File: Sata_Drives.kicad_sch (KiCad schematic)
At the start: 66 parts

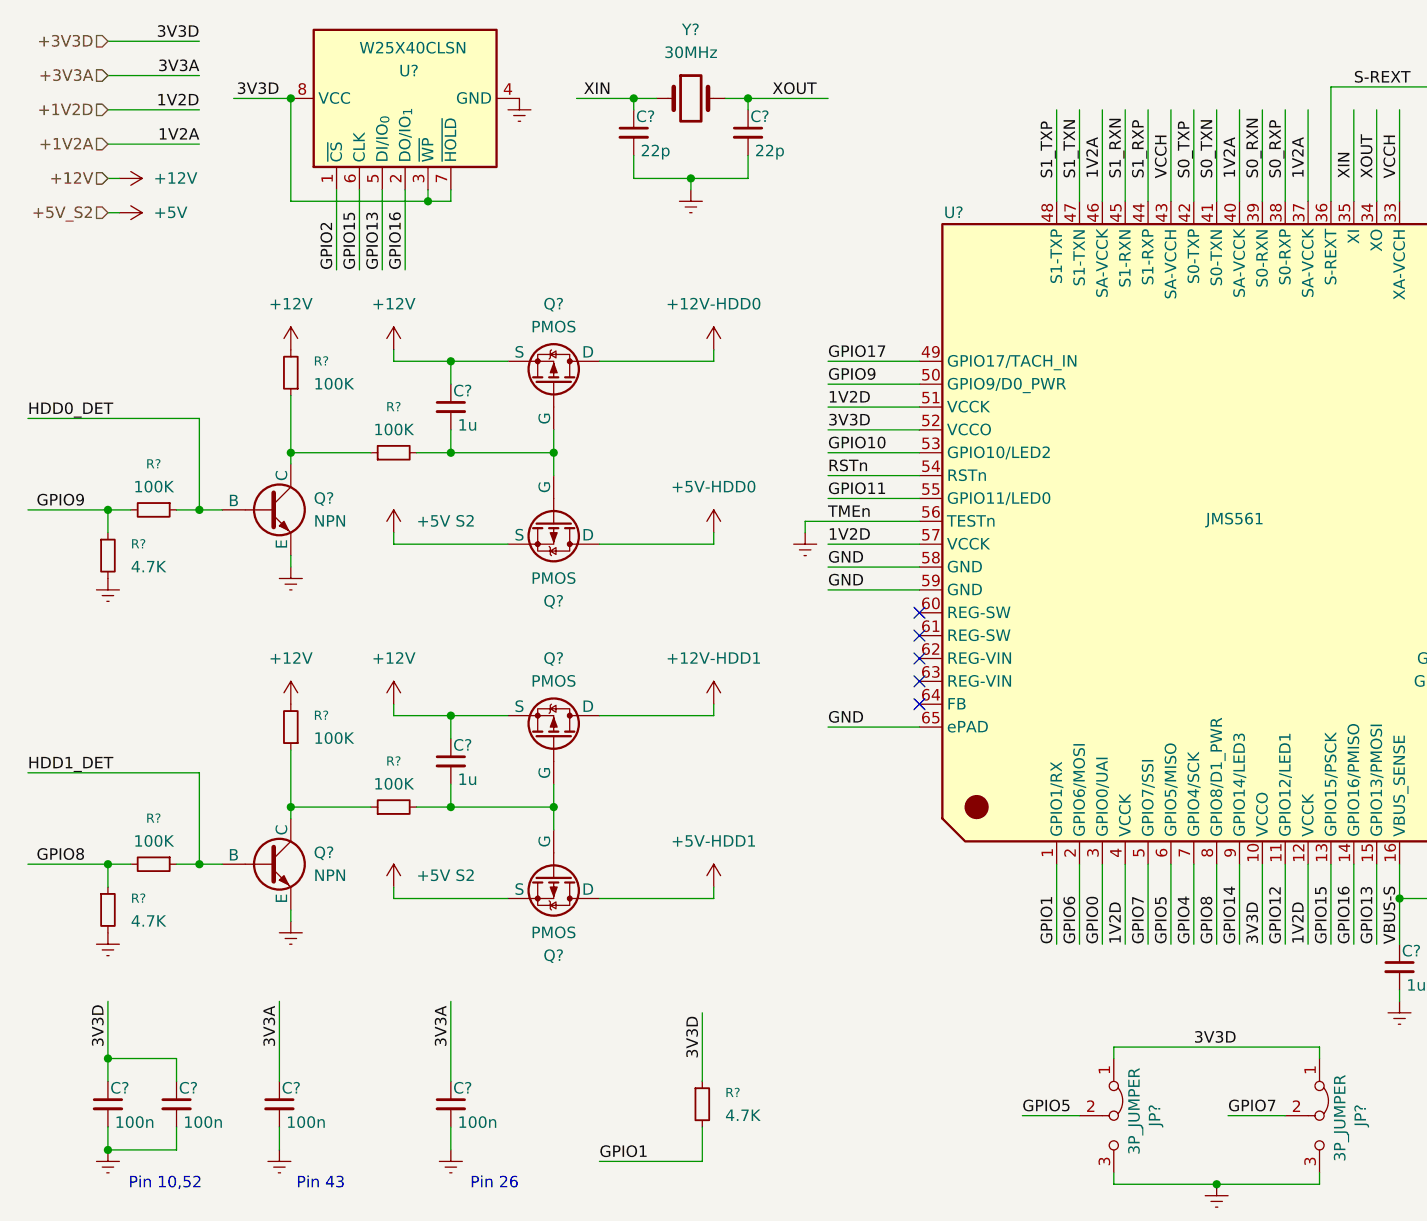
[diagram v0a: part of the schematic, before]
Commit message: Removed Ethernet
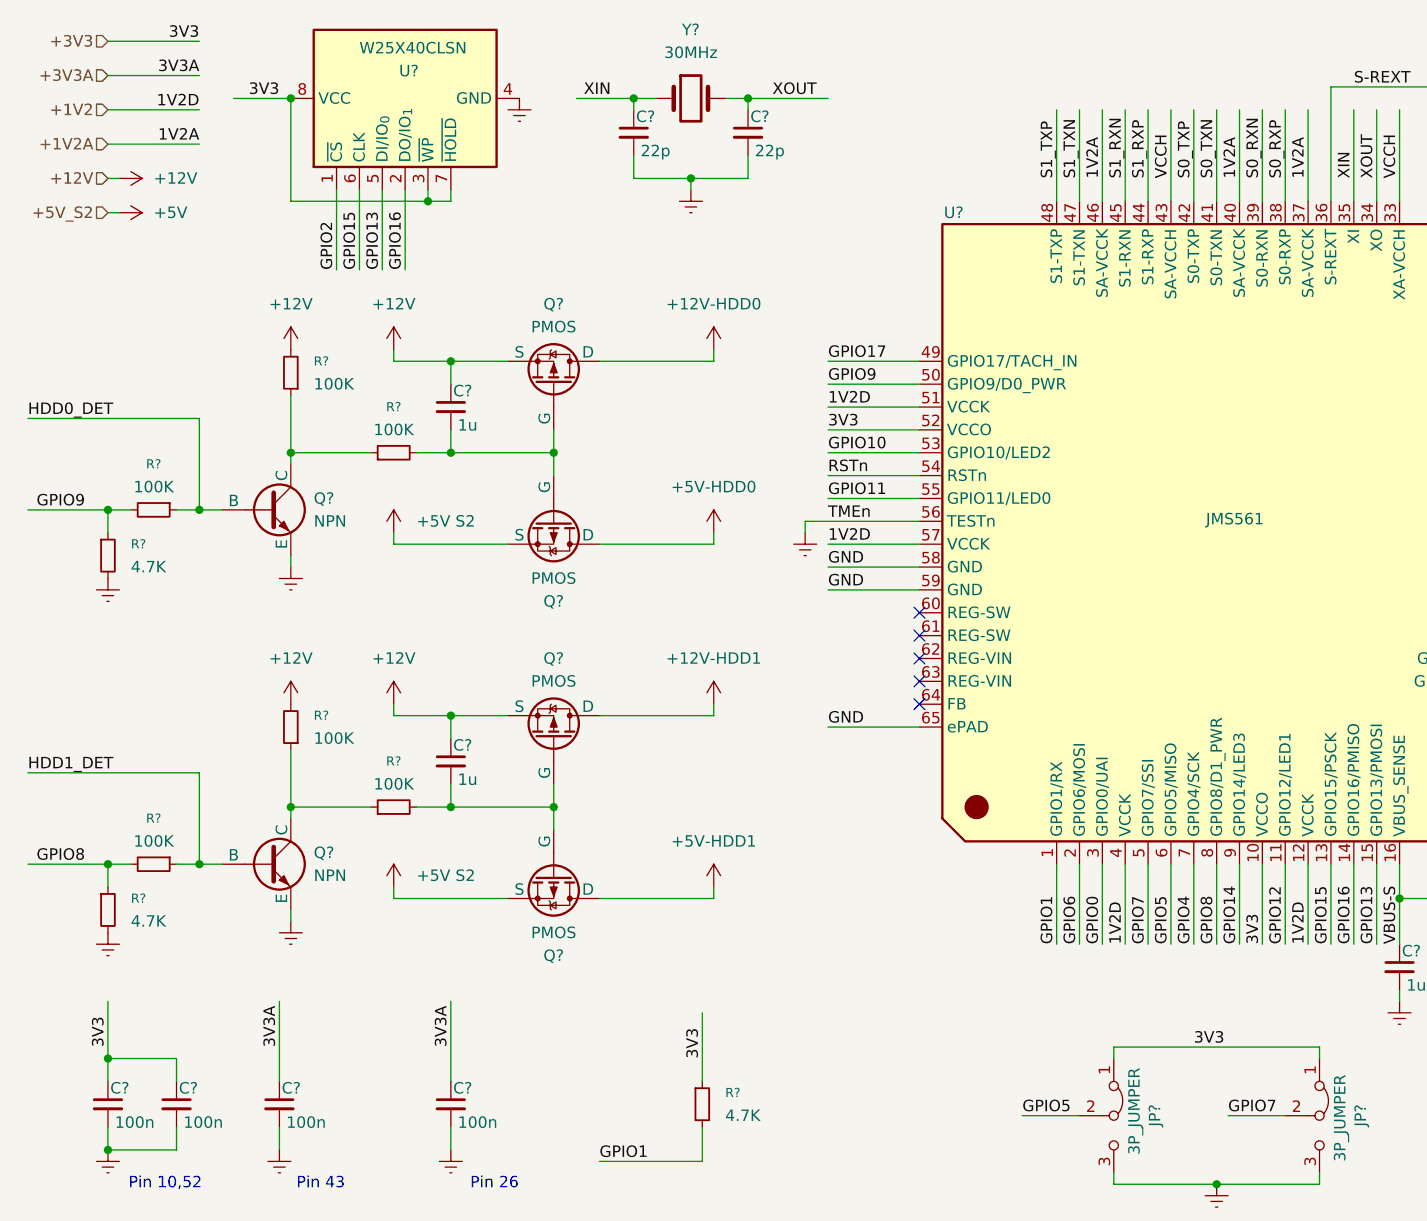
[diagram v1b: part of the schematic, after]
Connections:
- net +1V2D renamed +1V2
- net +3V3D renamed +3V3
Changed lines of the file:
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@@
 		)
 	)
-	(label "3V3D"
+	(label "3V3"
 		(at 34.29 15.24 180)
 		(effects
@@
 		)
 	)
-	(label "3V3D"
+	(label "3V3"
 		(at 144.78 127 0)
 		(effects
@@
 		)
 	)
-	(label "3V3D"
+	(label "3V3"
 		(at 24.13 127 90)
 		(effects
@@
 		)
 	)
-	(label "3V3D"
+	(label "3V3"
 		(at 90.17 128.27 90)
 		(effects
@@
 		)
 	)
-	(label "3V3D"
+	(label "3V3"
 		(at 43.18 21.59 180)
 		(effects
@@
 		)
 	)
-	(label "3V3D"
+	(label "3V3"
 		(at 152.4 115.57 90)
 		(effects
@@
 		)
 	)
-	(label "3V3D"
+	(label "3V3"
 		(at 104.14 58.42 0)
 		(effects
@@
 		)
 	)
-	(hierarchical_label "+1V2D"
+	(hierarchical_label "+1V2"
 		(shape input)
 		(at 24.13 22.86 180)
@@
 		)
 	)
-	(hierarchical_label "+3V3D"
+	(hierarchical_label "+3V3"
 		(shape input)
 		(at 24.13 15.24 180)

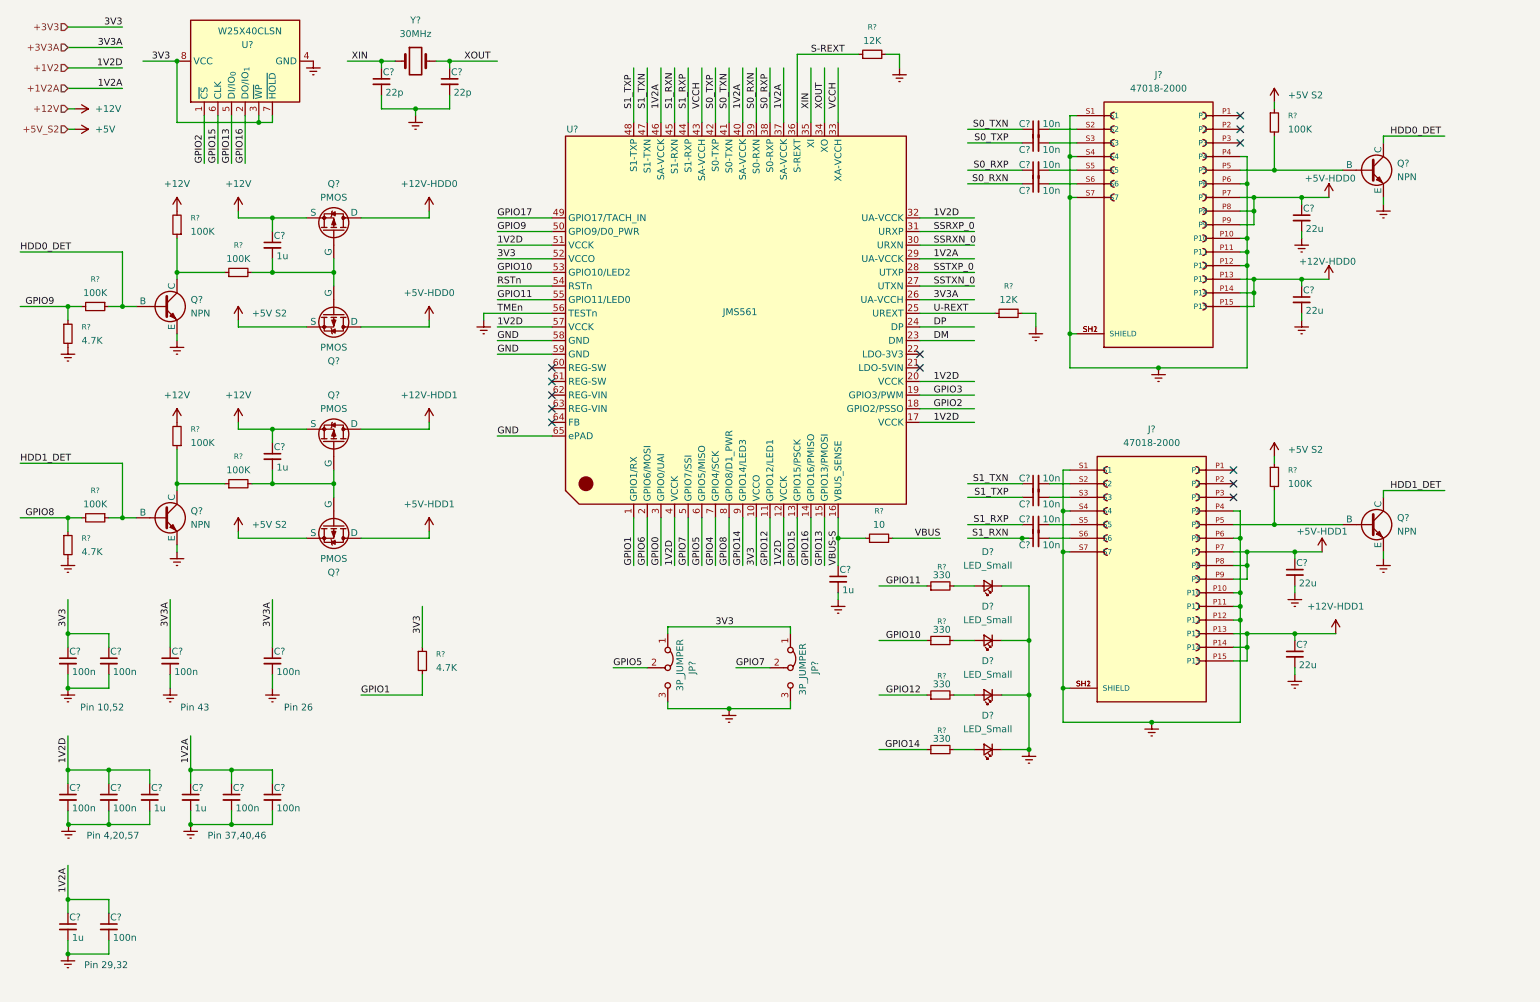
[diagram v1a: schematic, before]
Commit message: Sheets neatened
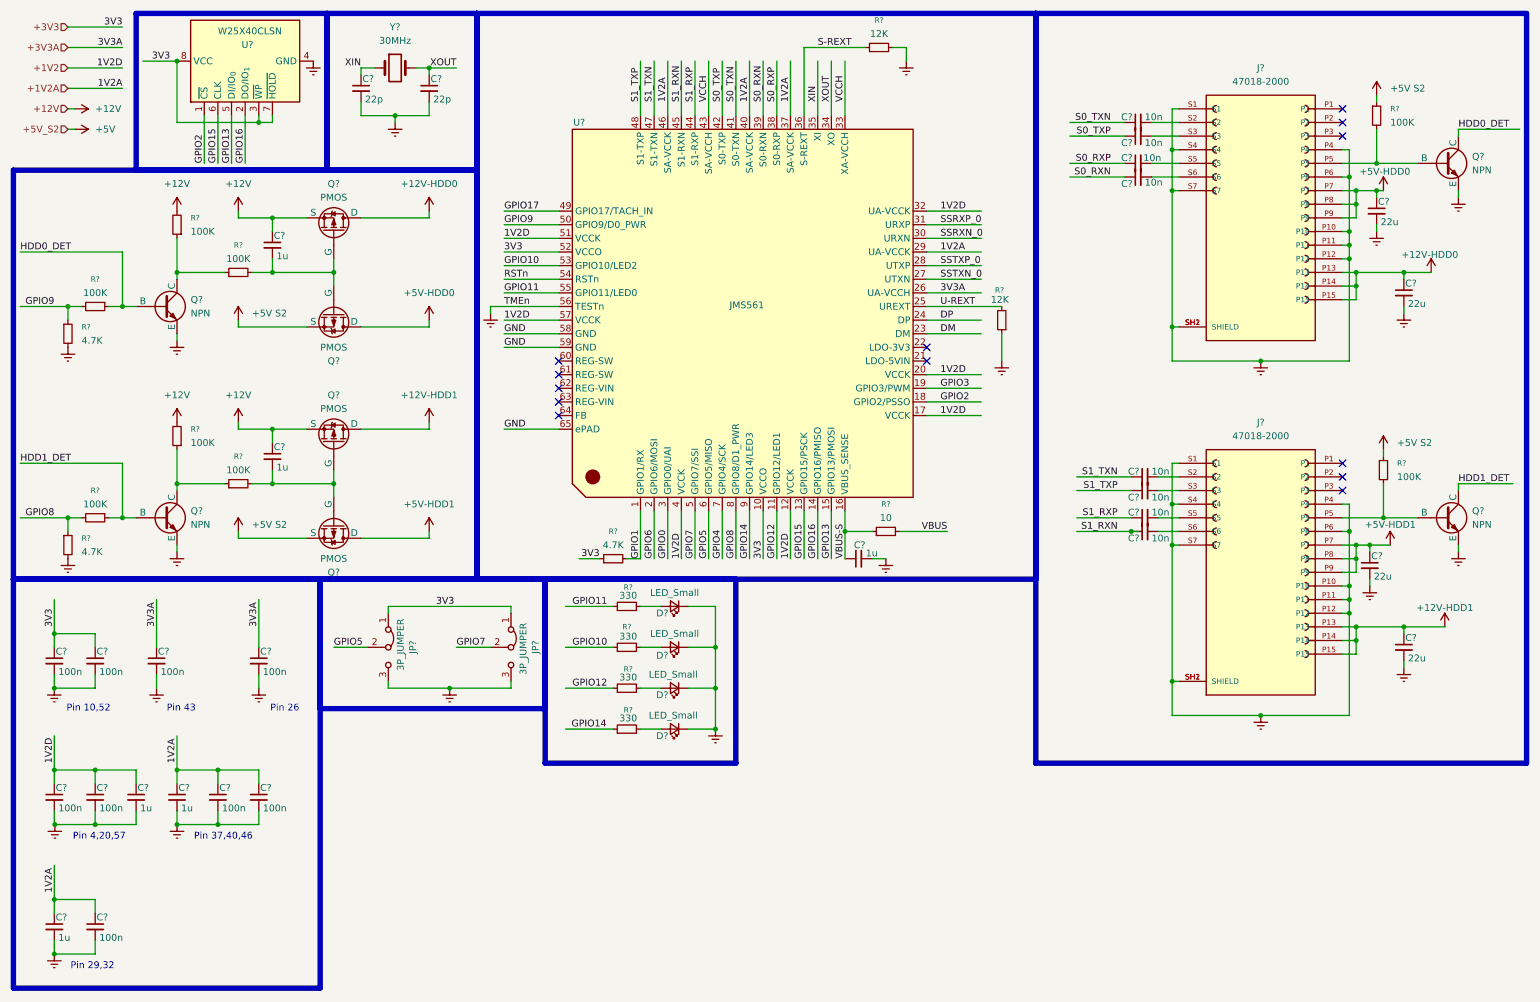
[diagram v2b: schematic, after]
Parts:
- removed C? (x9): 100n, symbol Device:C_Small
- removed C? (x3): 1u, symbol Device:C_Small
- removed D? (x4): LED_Small, symbol Device:LED_Small
- removed JP? (x2): 3P_JUMPER, symbol Jumper:Jumper_3_Bridged12
- removed R?: 4.7K, symbol Device:R_Small
- removed R? (x4): 330, symbol Device:R_Small
- added C? (x9): 100n, symbol Device:C_Small
- added C? (x3): 1u, symbol Device:C_Small
- added D? (x4): LED_Small, symbol Device:LED_Small
- added JP? (x2): 3P_JUMPER, symbol Jumper:Jumper_3_Bridged12
- added R? (x4): 330, symbol Device:R_Small
- added R?: 4.7K, symbol Device:R_Small
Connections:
- net +1V2: now also C?.1, C?.1, C?.1
- net +1V2A: now also C?.1, C?.1, C?.1, C?.1, C?.1
- net +3V3: now also C?.1, C?.1, JP?.1 (A), JP?.1 (A), R?.1
- net +3V3A: now also C?.1, C?.1
- net GPIO1: now also R?.2
- net GPIO10: now also R?.1
- net GPIO11: now also R?.1
- net GPIO12: now also R?.1
- net GPIO14: now also R?.1
- net GPIO5: now also JP?.2 (C)
- net GPIO7: now also JP?.2 (C)
- net U-REXT: now also R?.2; no longer R?.1
- new net: D?.2 (A), R?.2 (x4)
- new net: D?.1 (K), D?.1 (K), D?.1 (K), D?.1 (K)
- new net: C?.2, C?.2, C?.2 (x2)
- new net: C?.2, C?.2 (x2)
- new net: JP?.3 (B), JP?.3 (B)
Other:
- moved on the sheet: C?, J?, Q?, R?, U?, Y?

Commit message: More Fans
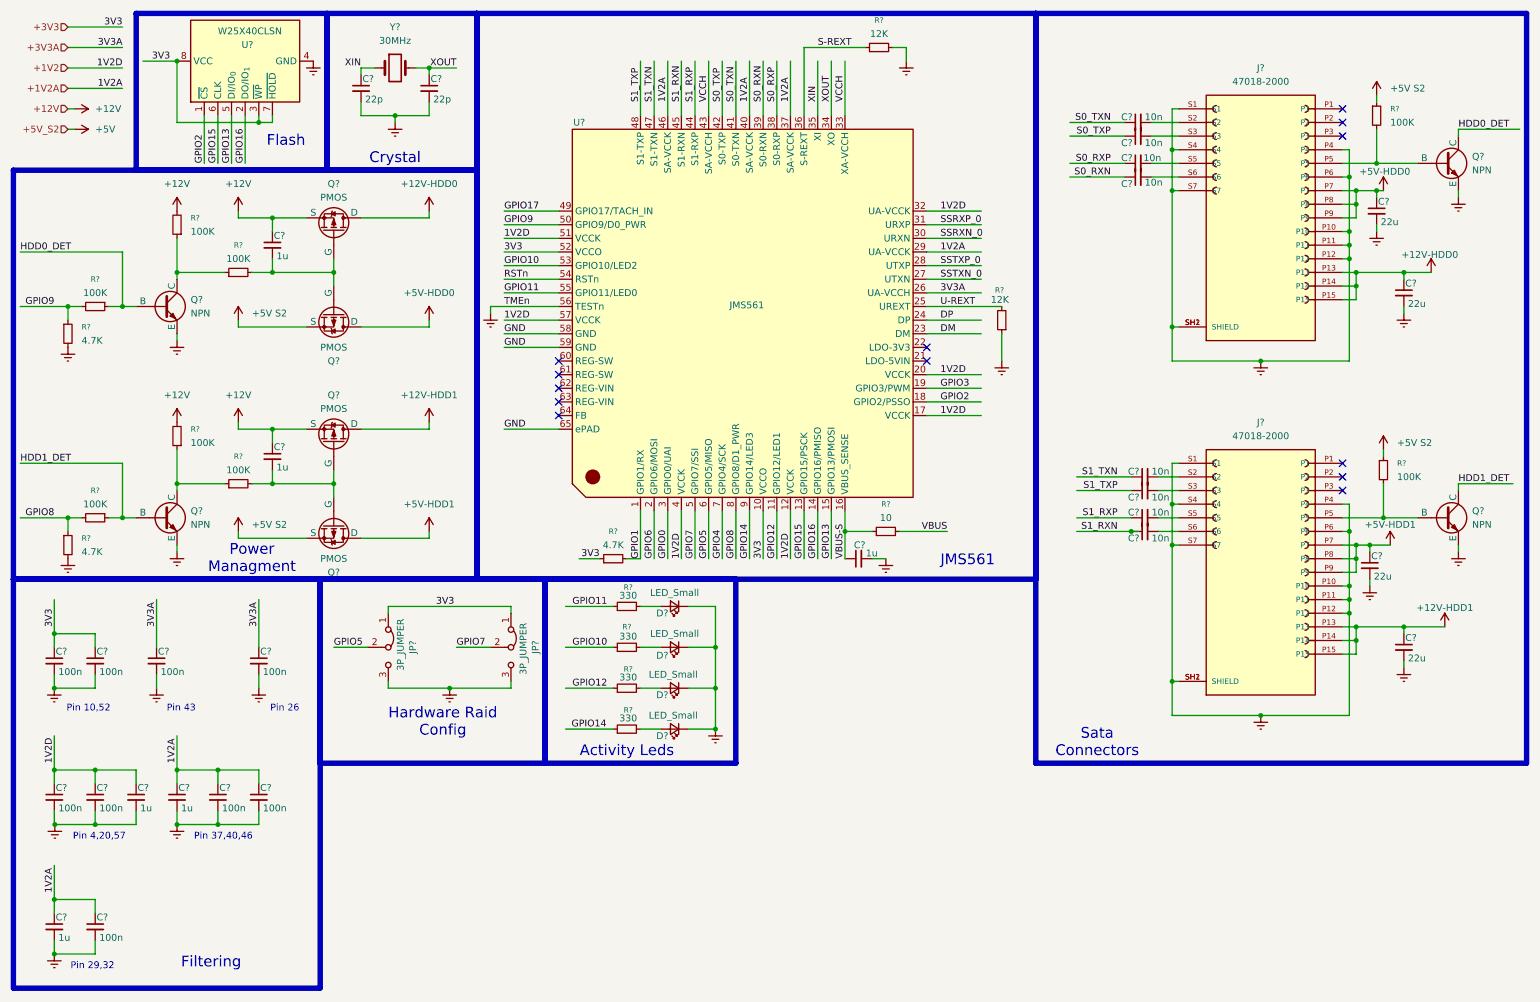
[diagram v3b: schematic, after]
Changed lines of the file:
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@@
 	(rectangle
 		(start 71.12 118.11)
-		(end 113.03 142.24)
+		(end 113.03 152.4)
 		(stroke
 			(width 1)
@@
 		)
 	)
+	(text_box "Filtering"
+		(exclude_from_sim no)
+		(at 36.83 182.88 0)
+		(size 27.94 9.525)
+		(margins 1.9049 1.9049 1.9049 1.9049)
+		(stroke
+			(width -0.0001)
+			(type solid)
+		)
+		(fill
+			(type none)
+		)
+		(effects
+			(font
+				(face "Times New Roman")
+				(size 2 2)
+				(thickness 0.3175)
+				(color 162 22 34 1)
+			)
+			(justify bottom)
+		)
+	)
+	(text_box "Flash\n\n"
+		(exclude_from_sim no)
+		(at 50.8 33.02 0)
+		(size 27.94 9.525)
+		(margins 1.9049 1.9049 1.9049 1.9049)
+		(stroke
+			(width -0.0001)
+			(type solid)
+		)
+		(fill
+			(type none)
+		)
+		(effects
+			(font
+				(face "Times New Roman")
+				(size 2 2)
+				(thickness 0.3175)
+				(color 162 22 34 1)
+			)
+			(justify bottom)
+		)
+	)
+	(text_box "JMS561"
+		(exclude_from_sim no)
+		(at 177.8 107.95 0)
+		(size 27.94 9.525)
+		(margins 1.9049 1.9049 1.9049 1.9049)
+		(stroke
+			(width -0.0001)
+			(type solid)
+		)
+		(fill
+			(type none)
+		)
+		(effects
+			(font
+				(face "Times New Roman")
+				(size 2 2)
+				(thickness 0.3175)
+				(color 162 22 34 1)
+			)
+			(justify bottom)
+		)
+	)
+	(text_box "Sata Connectors\n"
+		(exclude_from_sim no)
+		(at 201.93 143.51 0)
+		(size 27.94 9.525)
+		(margins 1.9049 1.9049 1.9049 1.9049)
+		(stroke
+			(width -0.0001)
+			(type solid)
+		)
+		(fill
+			(type none)
+		)
+		(effects
+			(font
+				(face "Times New Roman")
+				(size 2 2)
+				(thickness 0.3175)
+				(color 162 22 34 1)
+			)
+			(justify bottom)
+		)
+	)
+	(text_box "Hardware Raid \nConfig\n"
+		(exclude_from_sim no)
+		(at 80.01 139.7 0)
+		(size 27.94 9.525)
+		(margins 1.9049 1.9049 1.9049 1.9049)
+		(stroke
+			(width -0.0001)
+			(type solid)
+		)
+		(fill
+			(type none)
+		)
+		(effects
+			(font
+				(face "Times New Roman")
+				(size 2 2)
+				(thickness 0.3175)
+				(color 162 22 34 1)
+			)
+			(justify bottom)
+		)
+	)
+	(text_box "Activity Leds\n"
+		(exclude_from_sim no)
+		(at 114.3 143.51 0)
+		(size 27.94 9.525)
+		(margins 1.9049 1.9049 1.9049 1.9049)
+		(stroke
+			(width -0.0001)
+			(type solid)
+		)
+		(fill
+			(type none)
+		)
+		(effects
+			(font
+				(face "Times New Roman")
+				(size 2 2)
+				(thickness 0.3175)
+				(color 162 22 34 1)
+			)
+			(justify bottom)
+		)
+	)
+	(text_box "Power Managment\n"
+		(exclude_from_sim no)
+		(at 44.45 109.22 0)
+		(size 27.94 9.525)
+		(margins 1.9049 1.9049 1.9049 1.9049)
+		(stroke
+			(width -0.0001)
+			(type solid)
+		)
+		(fill
+			(type none)
+		)
+		(effects
+			(font
+				(face "Times New Roman")
+				(size 2 2)
+				(thickness 0.3175)
+				(color 162 22 34 1)
+			)
+			(justify bottom)
+		)
+	)
+	(text_box "Crystal\n"
+		(exclude_from_sim no)
+		(at 71.12 33.02 0)
+		(size 27.94 9.525)
+		(margins 1.9049 1.9049 1.9049 1.9049)
+		(stroke
+			(width -0.0001)
+			(type solid)
+		)
+		(fill
+			(type none)
+		)
+		(effects
+			(font
+				(face "Times New Roman")
+				(size 2 2)
+				(thickness 0.3175)
+				(color 162 22 34 1)
+			)
+			(justify bottom)
+		)
+	)
